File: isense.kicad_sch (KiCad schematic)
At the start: 0 parts

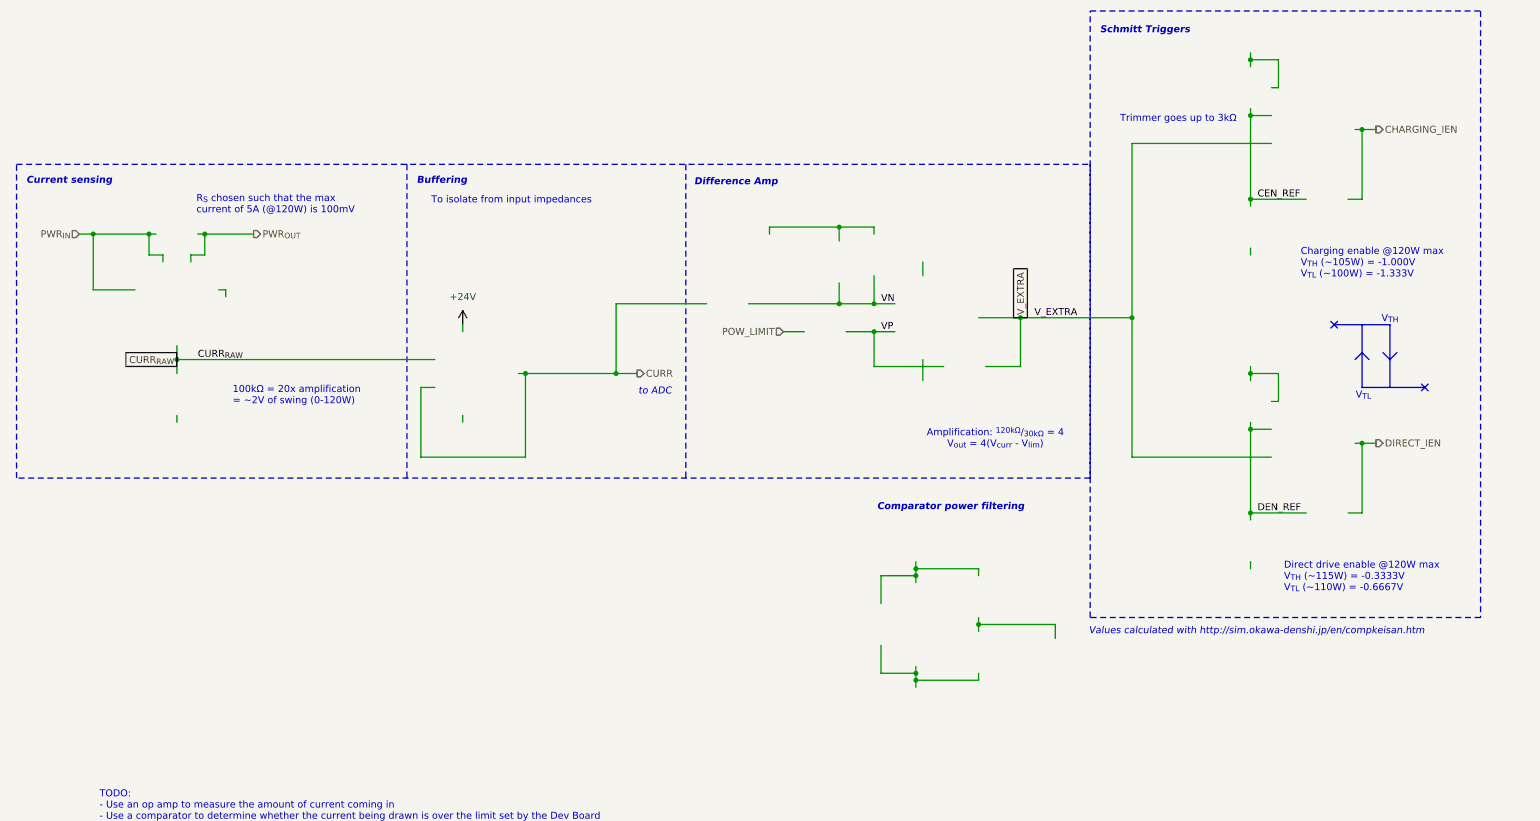
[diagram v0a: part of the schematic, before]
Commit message: restore broken current sense schematic
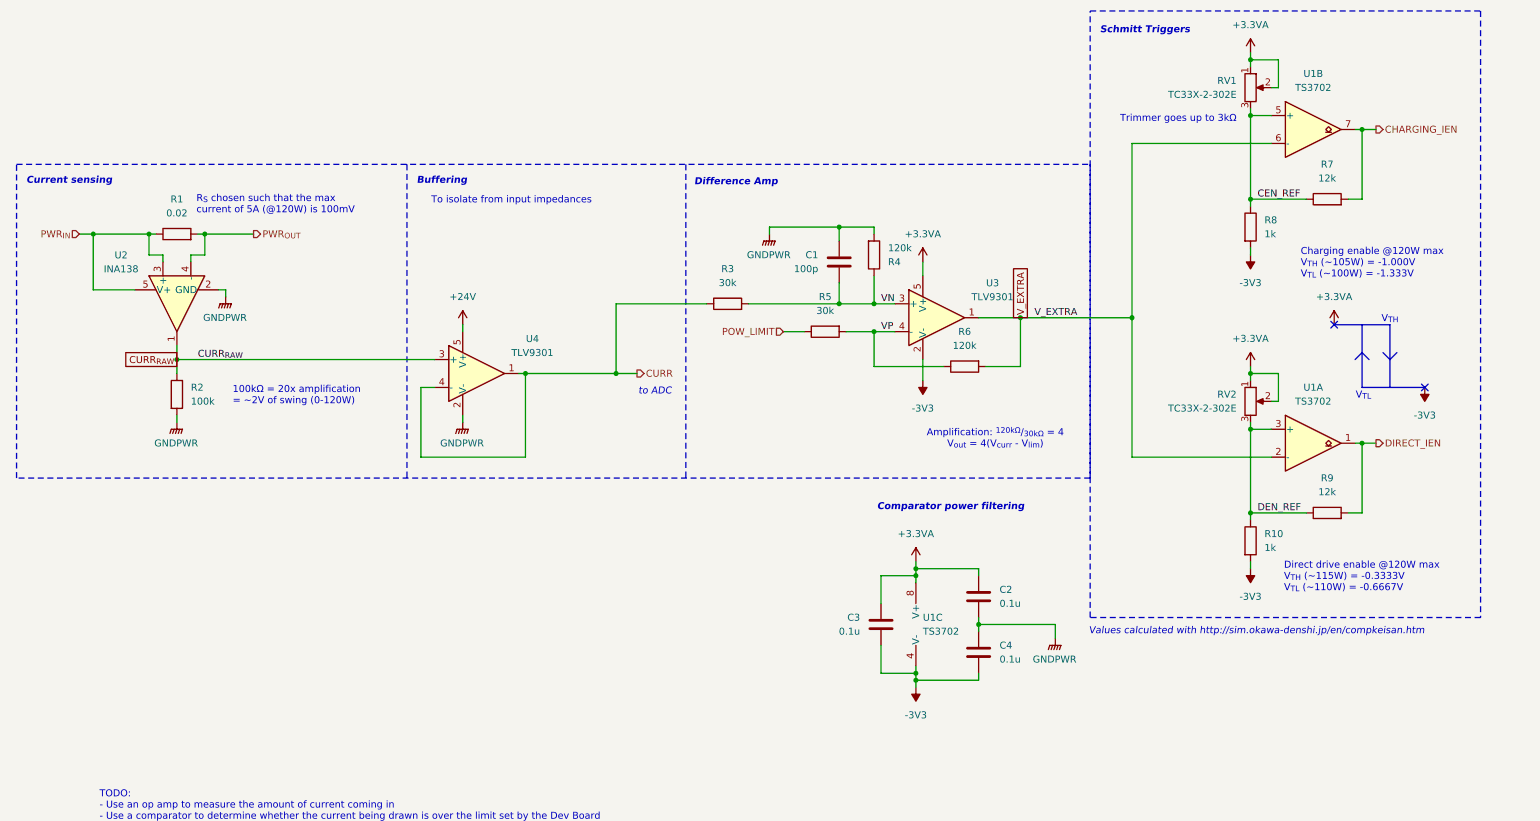
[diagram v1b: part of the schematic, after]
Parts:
- added C1: 100p, Capacitor_SMD:C_0603_1608Metric_Pad1.08x0.95mm_HandSolder, symbol Device:C
- added C2, C3, C4: 0.1u, Capacitor_SMD:C_0603_1608Metric_Pad1.08x0.95mm_HandSolder, symbol Device:C
- added R1: 0.02, Resistor_SMD:R_0805_2012Metric_Pad1.20x1.40mm_HandSolder, symbol Device:R
- added R10, R8: 1k, Resistor_SMD:R_0603_1608Metric_Pad0.98x0.95mm_HandSolder, symbol Device:R
- added R2: 100k, Resistor_SMD:R_0603_1608Metric_Pad0.98x0.95mm_HandSolder, symbol Device:R
- added R3, R5: 30k, Resistor_SMD:R_0603_1608Metric_Pad0.98x0.95mm_HandSolder, symbol Device:R
- added R4, R6: 120k, Resistor_SMD:R_0603_1608Metric_Pad0.98x0.95mm_HandSolder, symbol Device:R
- added R7, R9: 12k, Resistor_SMD:R_0603_1608Metric_Pad0.98x0.95mm_HandSolder, symbol Device:R
- added RV1, RV2: TC33X-2-302E, Potentiometer_SMD:Potentiometer_Bourns_TC33X_Vertical, symbol Device:R_Potentiometer
- added U1: TS3702, Package_SO:SOIC-8_3.9x4.9mm_P1.27mm, symbol ! Robomaster ICs:TS3902
- added U2: INA138, Package_TO_SOT_SMD:SOT-23_Handsoldering, symbol Amplifier_Current:INA138
- added U3, U4: TLV9301, Package_TO_SOT_SMD:SOT-23-5_HandSoldering, symbol Amplifier_Operational:LM321
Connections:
- net +24V: now also U4.5 (V+)
- net CEN_REF: now also R7.1, R8.1, RV1.3, U1.5 (+)
- net CHARGING_IEN: now also R7.2, U1.7
- net CURR: now also R3.1, U4.1, U4.4 (-)
- net CURR_{RAW}: now also R2.1, U2.1, U4.3 (+)
- net DEN_REF: now also R10.1, R9.1, RV2.3, U1.3 (+)
- net DIRECT_IEN: now also R9.2, U1.1
- net POW_LIMIT: now also R5.1
- net PWR_{IN}: now also R1.1, U2.3 (+), U2.5 (V+)
- net PWR_{OUT}: now also R1.2, U2.4 (-)
- net VN: now also C1.2, R3.2, R4.1, U3.3 (+)
- net VP: now also R5.2, R6.1, U3.4 (-)
- net V_EXTRA: now also R6.2, U1.2 (-), U1.6 (-), U3.1
- new net +3.3VA: C2.2, C3.2, RV1.1, RV1.2, RV2.1, RV2.2, U1.8 (V+), U3.5 (V+)
- new net -3V3: C3.1, C4.1, R10.2, R8.2, U1.4 (V-), U3.2 (V-)
- new net GNDPWR: C1.1, C2.1, C4.2, R2.2, R4.2, U2.2 (GND), U4.2 (V-)

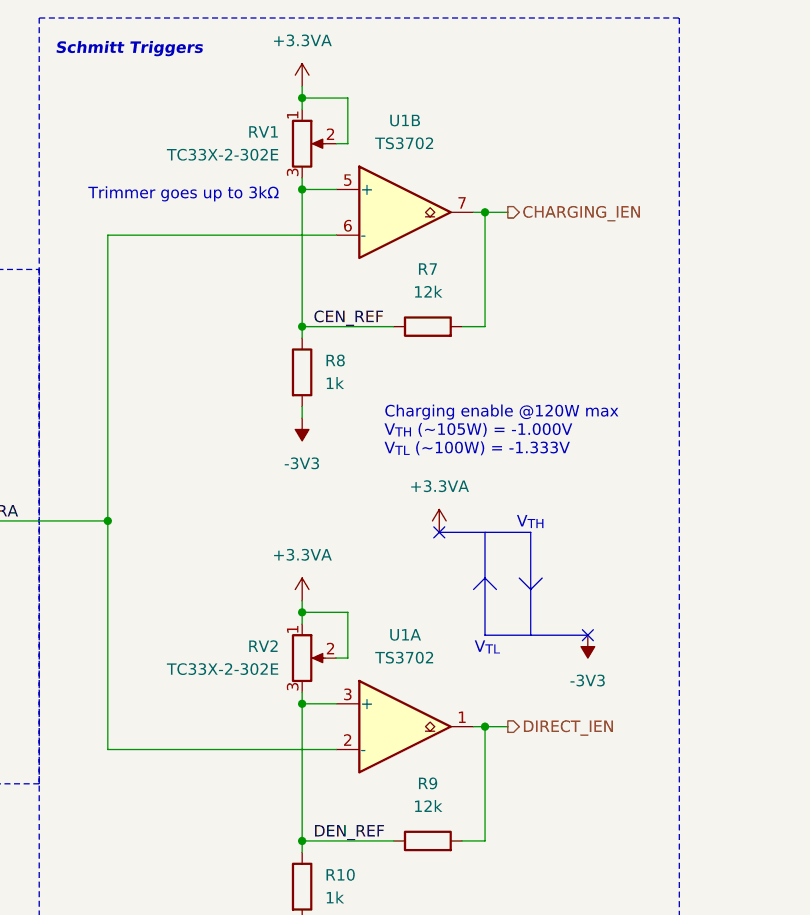
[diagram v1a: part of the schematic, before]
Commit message: current sense tweaks
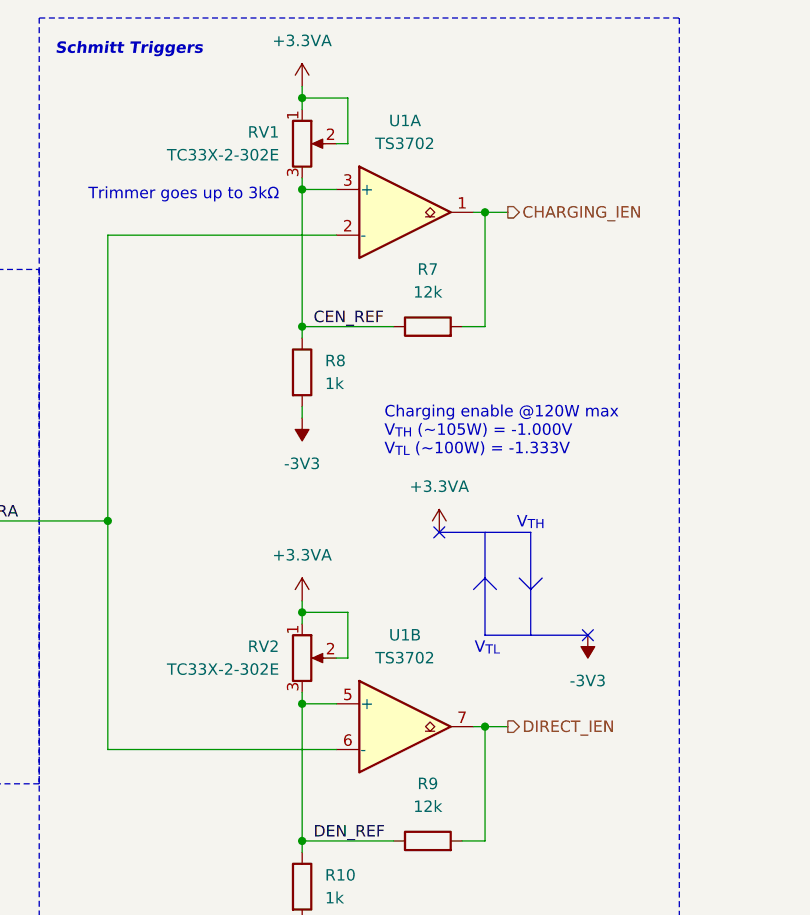
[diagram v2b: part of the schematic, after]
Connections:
- net CEN_REF: now also U1.3 (+); no longer U1.5 (+)
- net CHARGING_IEN: now also U1.1; no longer U1.7
- net DEN_REF: now also U1.5 (+); no longer U1.3 (+)
- net DIRECT_IEN: now also U1.7; no longer U1.1
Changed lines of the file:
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@@
-	)
-	(symbol
-		(lib_id "! Robomaster ICs:TS3902")
-		(at 251.46 102.87 0)
-		(unit 1)
-		(exclude_from_sim no)
-		(in_bom yes)
-		(on_board yes)
-		(dnp no)
-		(fields_autoplaced yes)
-		(property "Reference" "U1"
-			(at 251.46 92.71 0)
-			(effects
-				(font
-					(size 1.27 1.27)
-				)
-			)
-		)
-		(property "Value" "TS3702"
-			(at 251.46 95.25 0)
-			(effects
-				(font
-					(size 1.27 1.27)
-				)
-			)
-		)
-		(property "Footprint" "Package_SO:SOIC-8_3.9x4.9mm_P1.27mm"
-			(at 251.46 102.87 0)
-			(effects
-				(font
-					(size 1.27 1.27)
-				)
-				(hide yes)
-			)
-		)
-		(property "Datasheet" "https://www.mouser.com/datasheet/2/389/ts3702-1852552.pdf"
-			(at 251.46 102.87 0)
-			(effects
-				(font
-					(size 1.27 1.27)
-				)
-				(hide yes)
-			)
-		)
-		(property "Description" "Micropower dual CMOS voltage comparator"
-			(at 251.46 102.87 0)
-			(effects
-				(font
-					(size 1.27 1.27)
-				)
-				(hide yes)
-			)
-		)
-		(pin "3"
-		)
-		(pin "6"
-		)
-		(pin "8"
-		)
-		(pin "5"
-		)
-		(pin "1"
-		)
-		(pin "4"
-		)
-		(pin "7"
-		)
-		(pin "2"
-		)
-		(instances
-			(project "Current Sense Rev1"
-				(path "/d149d1fa-5de7-4dc0-b1ef-e9c4223d2865/d74a941e-a2f2-4038-9bd8-2d6a304e330c"
-					(reference "U1")
-					(unit 1)
-				)
-			)
-		)
 	)
 	(symbol
@@
 				(path "/d149d1fa-5de7-4dc0-b1ef-e9c4223d2865/d74a941e-a2f2-4038-9bd8-2d6a304e330c"
 					(reference "C2")
+					(unit 1)
+				)
+			)
+		)
+	)
+	(symbol
+		(lib_id "! Robomaster ICs:TS3902")
+		(at 251.46 45.72 0)
+		(unit 1)
+		(exclude_from_sim no)
+		(in_bom yes)
+		(on_board yes)
+		(dnp no)
+		(fields_autoplaced yes)
+		(property "Reference" "U1"
+			(at 251.46 35.56 0)
+			(effects
+				(font
+					(size 1.27 1.27)
+				)
+			)
+		)
+		(property "Value" "TS3702"
+			(at 251.46 38.1 0)
+			(effects
+				(font
+					(size 1.27 1.27)
+				)
+			)
+		)
+		(property "Footprint" "Package_SO:SOIC-8_3.9x4.9mm_P1.27mm"
+			(at 251.46 45.72 0)
+			(effects
+				(font
+					(size 1.27 1.27)
+				)
+				(hide yes)
+			)
+		)
+		(property "Datasheet" "https://www.mouser.com/datasheet/2/389/ts3702-1852552.pdf"
+			(at 251.46 45.72 0)
+			(effects
+				(font
+					(size 1.27 1.27)
+				)
+				(hide yes)
+			)
+		)
+		(property "Description" "Micropower dual CMOS voltage comparator"
+			(at 251.46 45.72 0)
+			(effects
+				(font
+					(size 1.27 1.27)
+				)
+				(hide yes)
+			)
+		)
+		(pin "3"
+		)
+		(pin "6"
+		)
+		(pin "8"
+		)
+		(pin "5"
+		)
+		(pin "1"
+		)
+		(pin "4"
+		)
+		(pin "7"
+		)
+		(pin "2"
+		)
+		(instances
+			(project "Current Sense Rev1"
+				(path "/d149d1fa-5de7-4dc0-b1ef-e9c4223d2865/d74a941e-a2f2-4038-9bd8-2d6a304e330c"
+					(reference "U1")
 					(unit 1)
 				)
@@
 	)
 	(symbol
+		(lib_id "! Robomaster ICs:TS3902")
+		(at 251.46 102.87 0)
+		(unit 2)
+		(exclude_from_sim no)
+		(in_bom yes)
+		(on_board yes)
+		(dnp no)
+		(fields_autoplaced yes)
+		(property "Reference" "U1"
+			(at 251.46 92.71 0)
+			(effects
+				(font
+					(size 1.27 1.27)
+				)
+			)
+		)
+		(property "Value" "TS3702"
+			(at 251.46 95.25 0)
+			(effects
+				(font
+					(size 1.27 1.27)
+				)
+			)
+		)
+		(property "Footprint" "Package_SO:SOIC-8_3.9x4.9mm_P1.27mm"
+			(at 251.46 102.87 0)
+			(effects
+				(font
+					(size 1.27 1.27)
+				)
+				(hide yes)
+			)
+		)
+		(property "Datasheet" "https://www.mouser.com/datasheet/2/389/ts3702-1852552.pdf"
+			(at 251.46 102.87 0)
+			(effects
+				(font
+					(size 1.27 1.27)
+				)
+				(hide yes)
+			)
+		)
+		(property "Description" "Micropower dual CMOS voltage comparator"
+			(at 251.46 102.87 0)
+			(effects
+				(font
+					(size 1.27 1.27)
+				)
+				(hide yes)
+			)
+		)
+		(pin "3"
+		)
+		(pin "6"
+		)
+		(pin "8"
+		)
+		(pin "5"
+		)
+		(pin "1"
+		)
+		(pin "4"
+		)
+		(pin "7"
+		)
+		(pin "2"
+		)
+		(instances
+			(project "Current Sense Rev1"
+				(path "/d149d1fa-5de7-4dc0-b1ef-e9c4223d2865/d74a941e-a2f2-4038-9bd8-2d6a304e330c"
+					(reference "U1")
+					(unit 2)
+				)
+			)
+		)
+	)
+	(symbol
 		(lib_id "power:+3.3VA")
 		(at 240.03 88.9 0)
@@
 				)
 			)
-		)
-	)
-	(symbol
-		(lib_id "! Robomaster ICs:TS3902")
-		(at 251.46 45.72 0)
-		(unit 2)
-		(exclude_from_sim no)
-		(in_bom yes)
-		(on_board yes)
-		(dnp no)
-		(fields_autoplaced yes)
-		(property "Reference" "U1"
-			(at 251.46 35.56 0)
-			(effects
-				(font
-					(size 1.27 1.27)
-				)
-			)
-		)
-		(property "Value" "TS3702"
-			(at 251.46 38.1 0)
-			(effects
-				(font
-					(size 1.27 1.27)
-				)
-			)
-		)
-		(property "Footprint" "Package_SO:SOIC-8_3.9x4.9mm_P1.27mm"
-			(at 251.46 45.72 0)
-			(effects
-				(font
-					(size 1.27 1.27)
-				)
-				(hide yes)
-			)
-		)
-		(property "Datasheet" "https://www.mouser.com/datasheet/2/389/ts3702-1852552.pdf"
-			(at 251.46 45.72 0)
-			(effects
-				(font
-					(size 1.27 1.27)
-				)
-				(hide yes)
-			)
-		)
-		(property "Description" "Micropower dual CMOS voltage comparator"
-			(at 251.46 45.72 0)
-			(effects
-				(font
-					(size 1.27 1.27)
-				)
-				(hide yes)
-			)
-		)
-		(pin "3"
-		)
-		(pin "6"
-		)
-		(pin "8"
-		)
-		(pin "5"
-		)
-		(pin "1"
-		)
-		(pin "4"
-		)
-		(pin "7"
-		)
-		(pin "2"
-		)
-		(instances
-			(project "Current Sense Rev1"
-				(path "/d149d1fa-5de7-4dc0-b1ef-e9c4223d2865/d74a941e-a2f2-4038-9bd8-2d6a304e330c"
-					(reference "U1")
-					(unit 2)
-				)
-			)

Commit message: modified tracks
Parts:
- U2: footprint Package_TO_SOT_SMD:SOT-23_Handsoldering -> Package_TO_SOT_SMD:SOT-23-5
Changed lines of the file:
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@@
 			)
 		)
-		(property "Footprint" "Package_TO_SOT_SMD:SOT-23_Handsoldering"
+		(property "Footprint" "Package_TO_SOT_SMD:SOT-23-5"
 			(at 44.45 77.47 0)
 			(effects

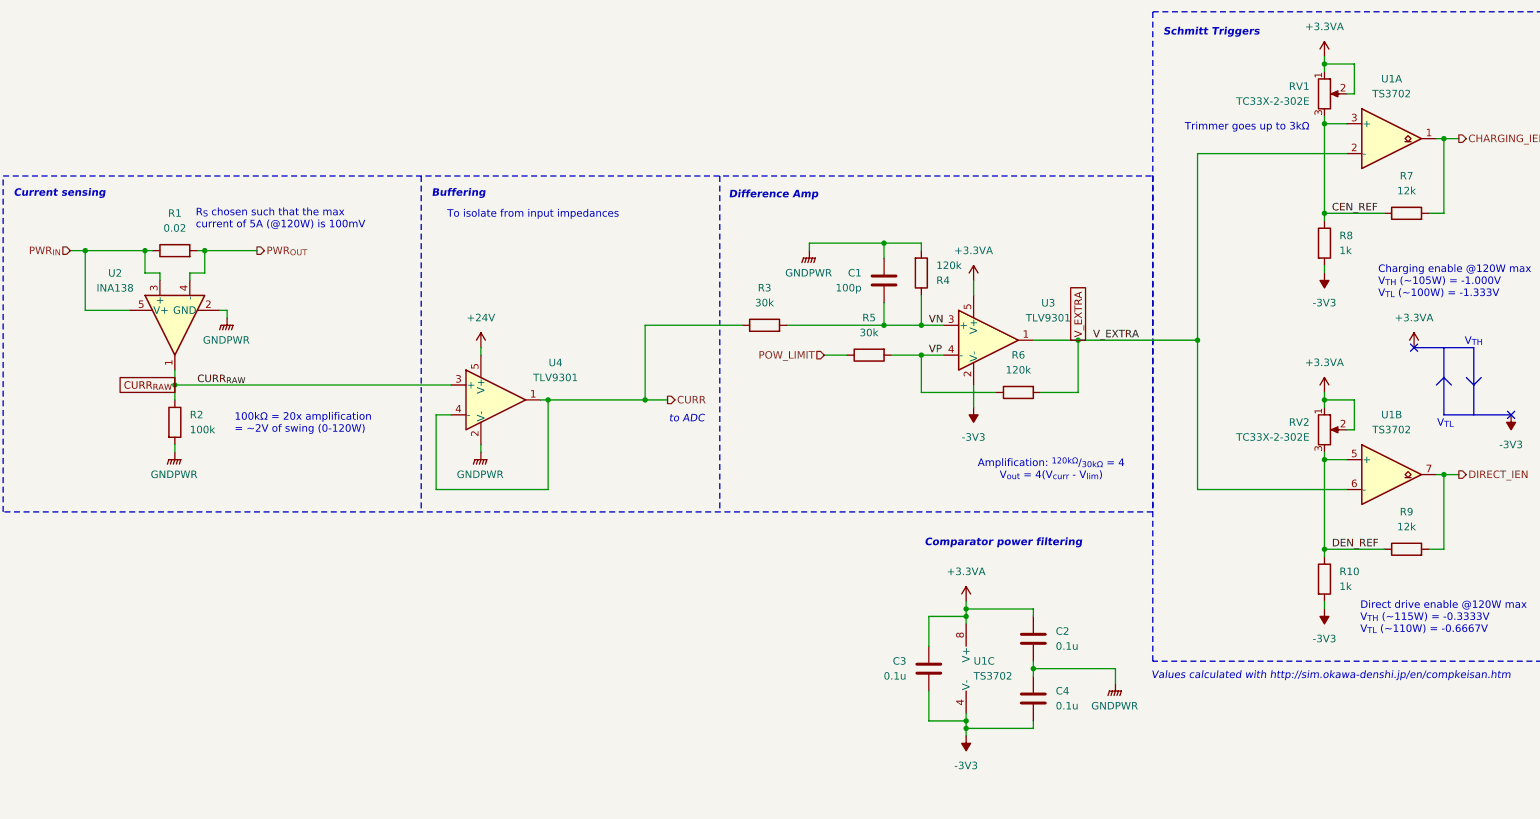
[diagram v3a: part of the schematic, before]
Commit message: Completed stage 2 schematic
+ added SPICE models for all the custom components
+ renumbered components
+ updated library with stage 2 symbols
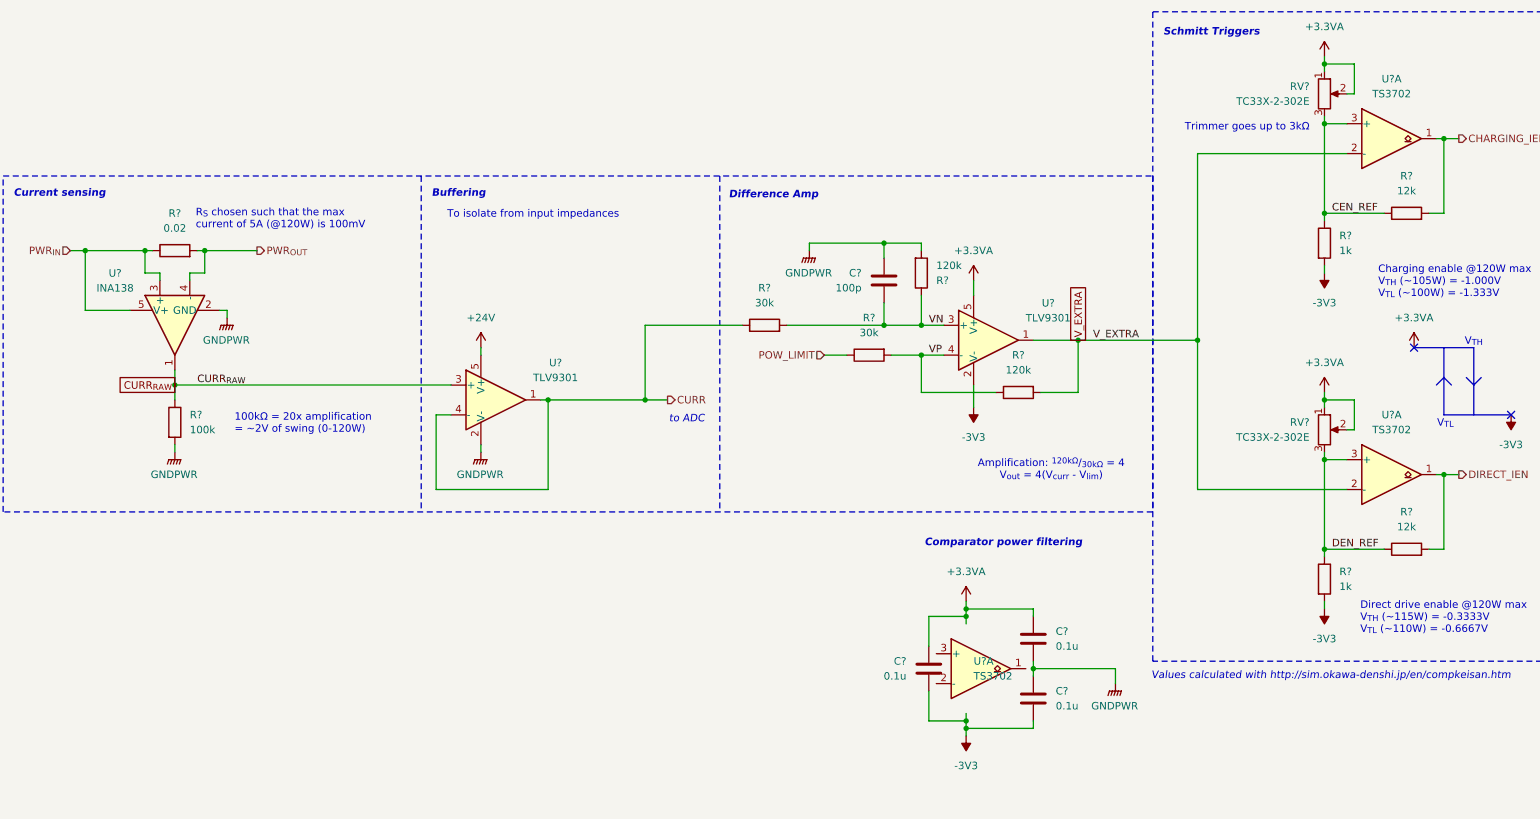
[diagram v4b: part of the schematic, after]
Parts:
- renumbered C1 to C?, C2 to C?, C3 to C?, C4 to C?, R1 to R?, R4 to R?, R6 to R?, R3 to R?, R7 to R?, R10 to R?, R2 to R?, R8 to R?, R9 to R?, R5 to R?, RV1 to RV?, RV2 to RV?, U1 to U?, U2 to U?, U3 to U?, U4 to U?
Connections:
- net +3.3VA: no longer U?.8 (V+)
- net -3V3: no longer U?.4 (V-)
- net DEN_REF: now also U?.3 (+); no longer U?.5 (+)
- net DIRECT_IEN: now also U?.1; no longer U?.7
- net V_EXTRA: now also U?.2 (-); no longer U?.6 (-)
